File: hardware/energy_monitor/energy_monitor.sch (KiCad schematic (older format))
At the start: 138 parts, among them J1 Screw_Terminal_01x03, J2 Audio-Jack-3, J3 Audio-Jack-3, J4 Audio-Jack-3, J5 Audio-Jack-3, J6 Audio-Jack-3, J7 Audio-Jack-3, J8 USB_OTG, Q1 MMBT2222, Q2 MMBT2222, U1 RAC04, U2 TPS730, U3 TPS723, U4 ADS131E08, U5 AP2112, U6 ESP-WROOM-32D, U7 CP2104

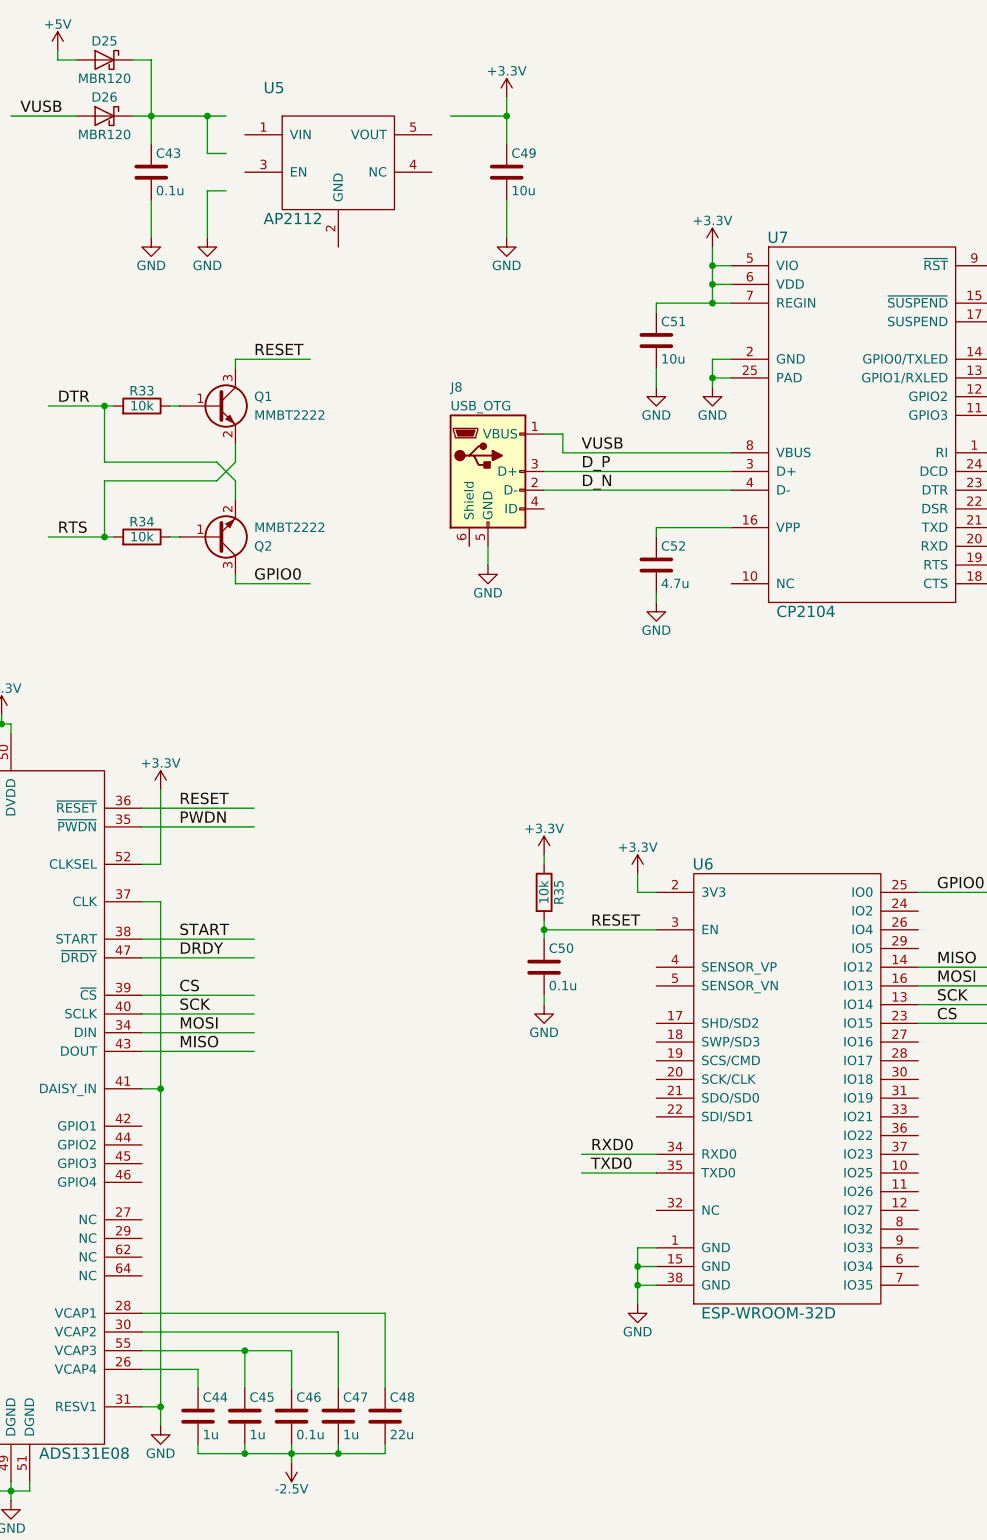
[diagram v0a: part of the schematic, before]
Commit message: Working on BOM and assigning footprints
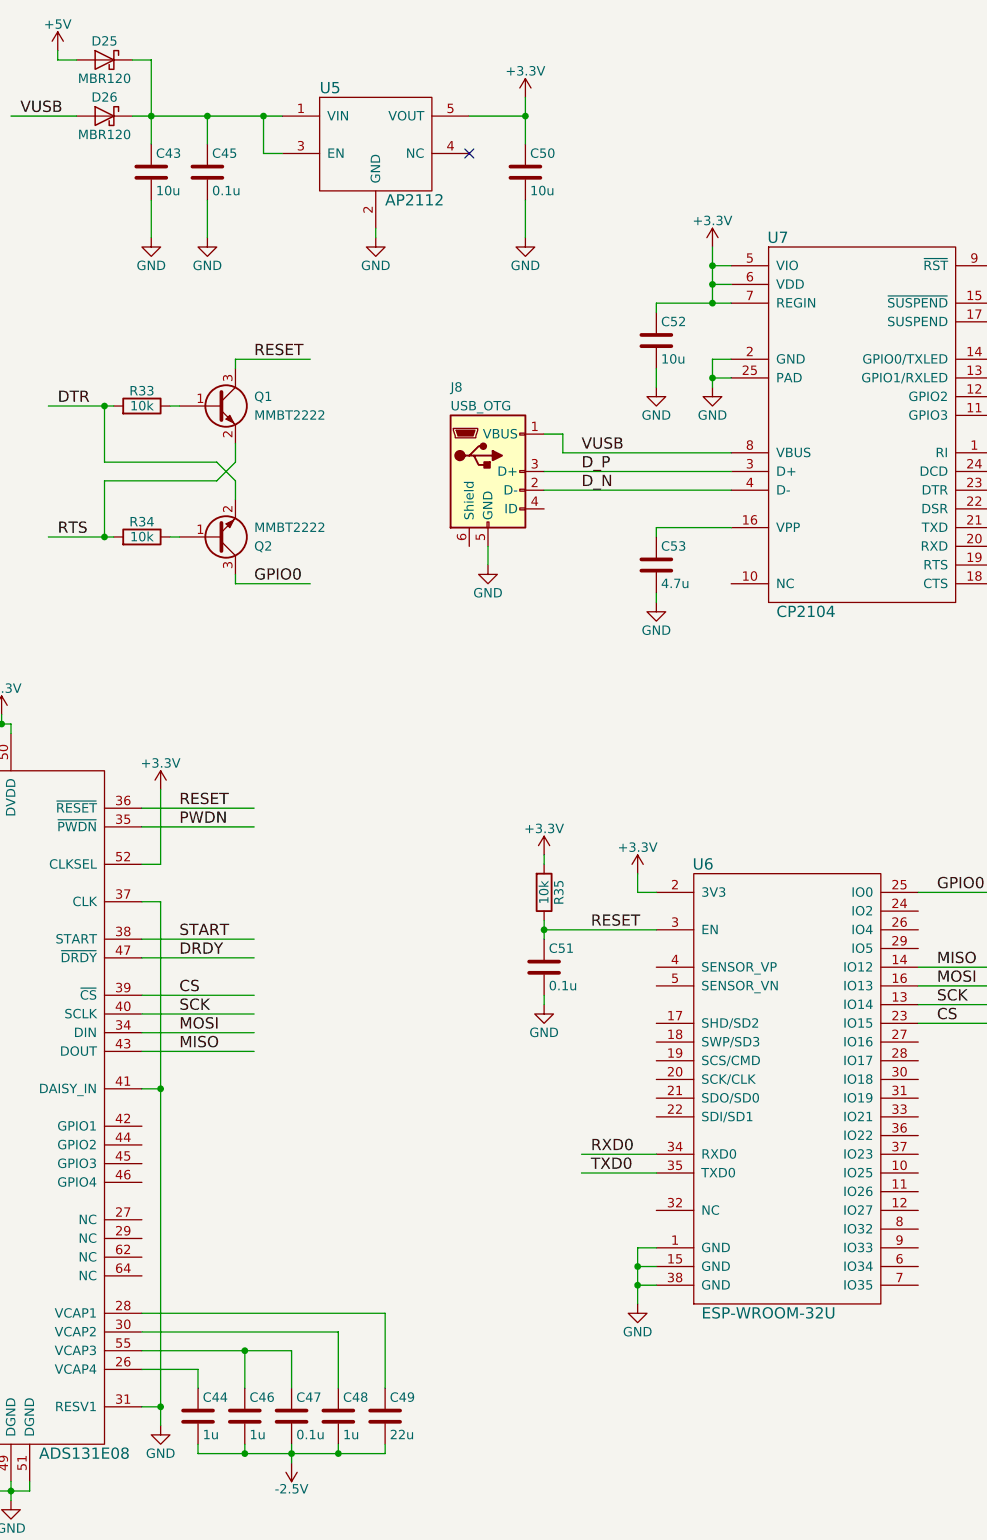
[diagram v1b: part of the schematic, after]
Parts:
- removed C49: 10u, symbol C
- added C48: 1u, Capacitors_SMD:C_0805, symbol C
- added C51: 0.1u, Capacitors_SMD:C_0603, symbol C
- C13, C14, C17, C32, C34, C37, C40, C42: footprint (none) -> Capacitors_SMD:C_0603; Part (none) -> 490-9691-1-ND; Source (none) -> DigiKey
- C15, C16: footprint (none) -> Capacitors_SMD:CP_Elec_6.3x5.8; Part (none) -> PCE3889CT-ND; Source (none) -> DigiKey
- C30, C36: footprint (none) -> Capacitors_SMD:C_0603; Part (none) -> 490-1520-1-ND; Source (none) -> DigiKey
- C31, C38: footprint (none) -> Capacitors_SMD:C_0805; Part (none) -> 490-11596-1-ND; Source (none) -> DigiKey
- C33: footprint (none) -> Capacitors_SMD:C_0805; Part (none) -> 490-5523-1-ND; Source (none) -> DigiKey
- C35, C39, C41, C44: footprint (none) -> Capacitors_SMD:C_0805; Part (none) -> 490-1691-1-ND; Source (none) -> DigiKey
- C43, C50: value 0.1u -> 10u; footprint (none) -> Capacitors_SMD:C_0805; Part (none) -> 490-5523-1-ND; Source (none) -> DigiKey
- C45, C47: value 1u -> 0.1u; footprint (none) -> Capacitors_SMD:C_0603; Part (none) -> 490-9691-1-ND; Source (none) -> DigiKey
- C46: value 0.1u -> 1u; footprint (none) -> Capacitors_SMD:C_0805; Part (none) -> 490-1691-1-ND; Source (none) -> DigiKey
- C49: renamed from C48; footprint (none) -> Capacitors_SMD:C_1206; Part (none) -> 490-8342-1-ND; Source (none) -> DigiKey
- C52: renamed from C51; footprint (none) -> Capacitors_SMD:C_0805; Part (none) -> 490-5523-1-ND; Source (none) -> DigiKey
- C53: renamed from C52; footprint (none) -> Capacitors_SMD:C_0805; Part (none) -> 490-5422-1-ND; Source (none) -> DigiKey
- D23, D27: Part (none) -> 160-1447-1-ND
- D24, D28: Part (none) -> 160-1435-1-ND
- D25, D26: footprint (none) -> footprint:SOD-123FL; Part (none) -> MBR120VLSFT3GOSCT-ND; Source (none) -> DigiKey
- F1, F2: footprint (none) -> Fuse_Holders_and_Fuses:Fuseholder5x20_horiz_open_inline_Type-I; Part (none) -> 486-2019-ND; Source (none) -> DigiKey
- J8: Part (none) -> H2959CT-ND; Source (none) -> DigiKey
- Q1, Q2: footprint (none) -> TO_SOT_Packages_SMD:SOT-23; Part (none) -> MMBT2222ALT3GOSCT-ND; Source (none) -> DigiKey
- R31, R32, R36, R37: Part (none) -> 311-1.00KHRCT-ND
- R33, R34, R35: footprint (none) -> Resistors_SMD:R_0603; Part (none) -> 311-10.0KHRCT-ND; Source (none) -> DigiKey
- RV1, RV2: footprint (none) -> Varistors:RV_Disc_D15.5_W6.8_P7.5
- U2, U3: footprint (none) -> TO_SOT_Packages_SMD:SOT-23-5
- U4: footprint (none) -> Housings_QFP:TQFP-64_10x10mm_Pitch0.5mm; Part (none) -> 296-43796-5-ND; Source (none) -> DigiKey
- U5: footprint (none) -> TO_SOT_Packages_SMD:SOT-23-5; Part (none) -> AP2112K-3.3TRG1DICT-ND; Source (none) -> DigiKey
- U6: value ESP-WROOM-32D -> ESP-WROOM-32U; footprint (none) -> footprint:ESP32-WROOM-32U; Source (none) -> DigiKey
- U7: footprint (none) -> Housings_DFN_QFN:QFN-24-1EP_4x4mm_Pitch0.5mm; Part (none) -> 336-2008-5-ND; Source (none) -> DigiKey
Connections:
- wire segments 430 -> 431
- no-connect marks 0 -> 1
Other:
- moved on the sheet: U5

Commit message: Working on footprints
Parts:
- removed J2, J3, J4, J5, J6, J7: Audio-Jack-3, symbol Audio-Jack-3
- added J2, J3, J4, J5, J6, J7: SJ1-3533NG, footprint:SJ1-3533NG, symbol SJ1-3533NG
- J1: Part 277-1118-ND -> 277-6062-ND

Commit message: Working on footprints
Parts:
- J1: footprint (none) -> footprint:1888690
- J8: footprint (none) -> footprint:UX60-MB-5ST
- U1: footprint (none) -> footprint:RAC04
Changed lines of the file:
@@
 F 0 "J1" H 900 1700 50  0000 C CNN
 F 1 "Screw_Terminal_01x03" H 900 1300 50  0001 C CNN
-F 2 "" H 900 1500 50  0001 C CNN
+F 2 "footprint:1888690" H 900 1500 50  0001 C CNN
 F 3 "" H 900 1500 50  0001 C CNN
 F 4 "DigiKey" H 900 1500 60  0001 C CNN "Source"
@@
 F 0 "U1" H 3000 2050 60  0000 L CNN
 F 1 "RAC04" H 3000 950 60  0000 L CNN
-F 2 "" H 3300 1500 60  0001 C CNN
+F 2 "footprint:RAC04" H 3300 1500 60  0001 C CNN
 F 3 "" H 3300 1500 60  0001 C CNN
 F 4 "DigiKey" H 3300 1500 60  0001 C CNN "Source"
@@
 F 0 "J8" H 12350 3550 50  0000 L CNN
 F 1 "USB_OTG" H 12350 3450 50  0000 L CNN
-F 2 "" H 12700 3050 50  0001 C CNN
+F 2 "footprint:UX60-MB-5ST" H 12700 3050 50  0001 C CNN
 F 3 "" H 12700 3050 50  0001 C CNN
 F 4 "DigiKey" H 12550 3100 60  0001 C CNN "Source"

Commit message: Working on layout
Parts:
- F1, F2: footprint Fuse_Holders_and_Fuses:Fuseholder5x20_horiz_open_inline_Type-I -> footprint:Fuse_Littelfuse-443; Part 486-2019-ND -> F2906CT-ND
- RV1, RV2: footprint Varistors:RV_Disc_D15.5_W6.8_P7.5 -> Varistors:RV_Disc_D12_W5_P7.5; Part 495-6609-ND -> P7207-ND
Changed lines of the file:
@@
 F 0 "F1" V 1630 1100 50  0000 C CNN
 F 1 "1A/300V" V 1475 1100 50  0000 C CNN
-F 2 "Fuse_Holders_and_Fuses:Fuseholder5x20_horiz_open_inline_Type-I" V 1480 1100 50  0001 C CNN
+F 2 "footprint:Fuse_Littelfuse-443" V 1480 1100 50  0001 C CNN
 F 3 "" H 1550 1100 50  0001 C CNN
 F 4 "DigiKey" H 1550 1100 60  0001 C CNN "Source"
-F 5 "486-2019-ND" H 1550 1100 60  0001 C CNN "Part"
+F 5 "F2906CT-ND" H 1550 1100 60  0001 C CNN "Part"
 	1    1550 1100
 	0    1    -1   0
@@
 F 0 "F2" V 1630 1900 50  0000 C CNN
 F 1 "1A/300V" V 1475 1900 50  0000 C CNN
-F 2 "Fuse_Holders_and_Fuses:Fuseholder5x20_horiz_open_inline_Type-I" V 1480 1900 50  0001 C CNN
+F 2 "footprint:Fuse_Littelfuse-443" V 1480 1900 50  0001 C CNN
 F 3 "" H 1550 1900 50  0001 C CNN
 F 4 "DigiKey" H 1550 1900 60  0001 C CNN "Source"
-F 5 "486-2019-ND" H 1550 1900 60  0001 C CNN "Part"
+F 5 "F2906CT-ND" H 1550 1900 60  0001 C CNN "Part"
 	1    1550 1900
 	0    1    -1   0
@@
 F 0 "RV1" H 2000 1350 50  0000 L CNN
 F 1 "MOV" H 2000 1250 50  0000 L CNN
-F 2 "Varistors:RV_Disc_D15.5_W6.8_P7.5" V 1830 1300 50  0001 C CNN
+F 2 "Varistors:RV_Disc_D12_W5_P7.5" V 1830 1300 50  0001 C CNN
 F 3 "" H 1900 1300 50  0001 C CNN
 F 4 "DigiKey" H 1900 1300 60  0001 C CNN "Source"
-F 5 "495-6609-ND" H 1900 1300 60  0001 C CNN "Part"
+F 5 "P7207-ND" H 1900 1300 60  0001 C CNN "Part"
 	1    1900 1300
 	1    0    0    -1
@@
 F 0 "RV2" H 2000 1750 50  0000 L CNN
 F 1 "MOV" H 2000 1650 50  0000 L CNN
-F 2 "Varistors:RV_Disc_D15.5_W6.8_P7.5" V 1830 1700 50  0001 C CNN
+F 2 "Varistors:RV_Disc_D12_W5_P7.5" V 1830 1700 50  0001 C CNN
 F 3 "" H 1900 1700 50  0001 C CNN
 F 4 "DigiKey" H 1900 1700 60  0001 C CNN "Source"
-F 5 "495-6609-ND" H 1900 1700 60  0001 C CNN "Part"
+F 5 "P7207-ND" H 1900 1700 60  0001 C CNN "Part"
 	1    1900 1700
 	1    0    0    -1

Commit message: Working on layout
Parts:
- C31, C38: value 2.2u -> 10u; Part 490-11596-1-ND -> 490-5523-1-ND
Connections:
- net labels added: GNDA, GNDD
- net labels removed: GND
- wire segments 431 -> 433

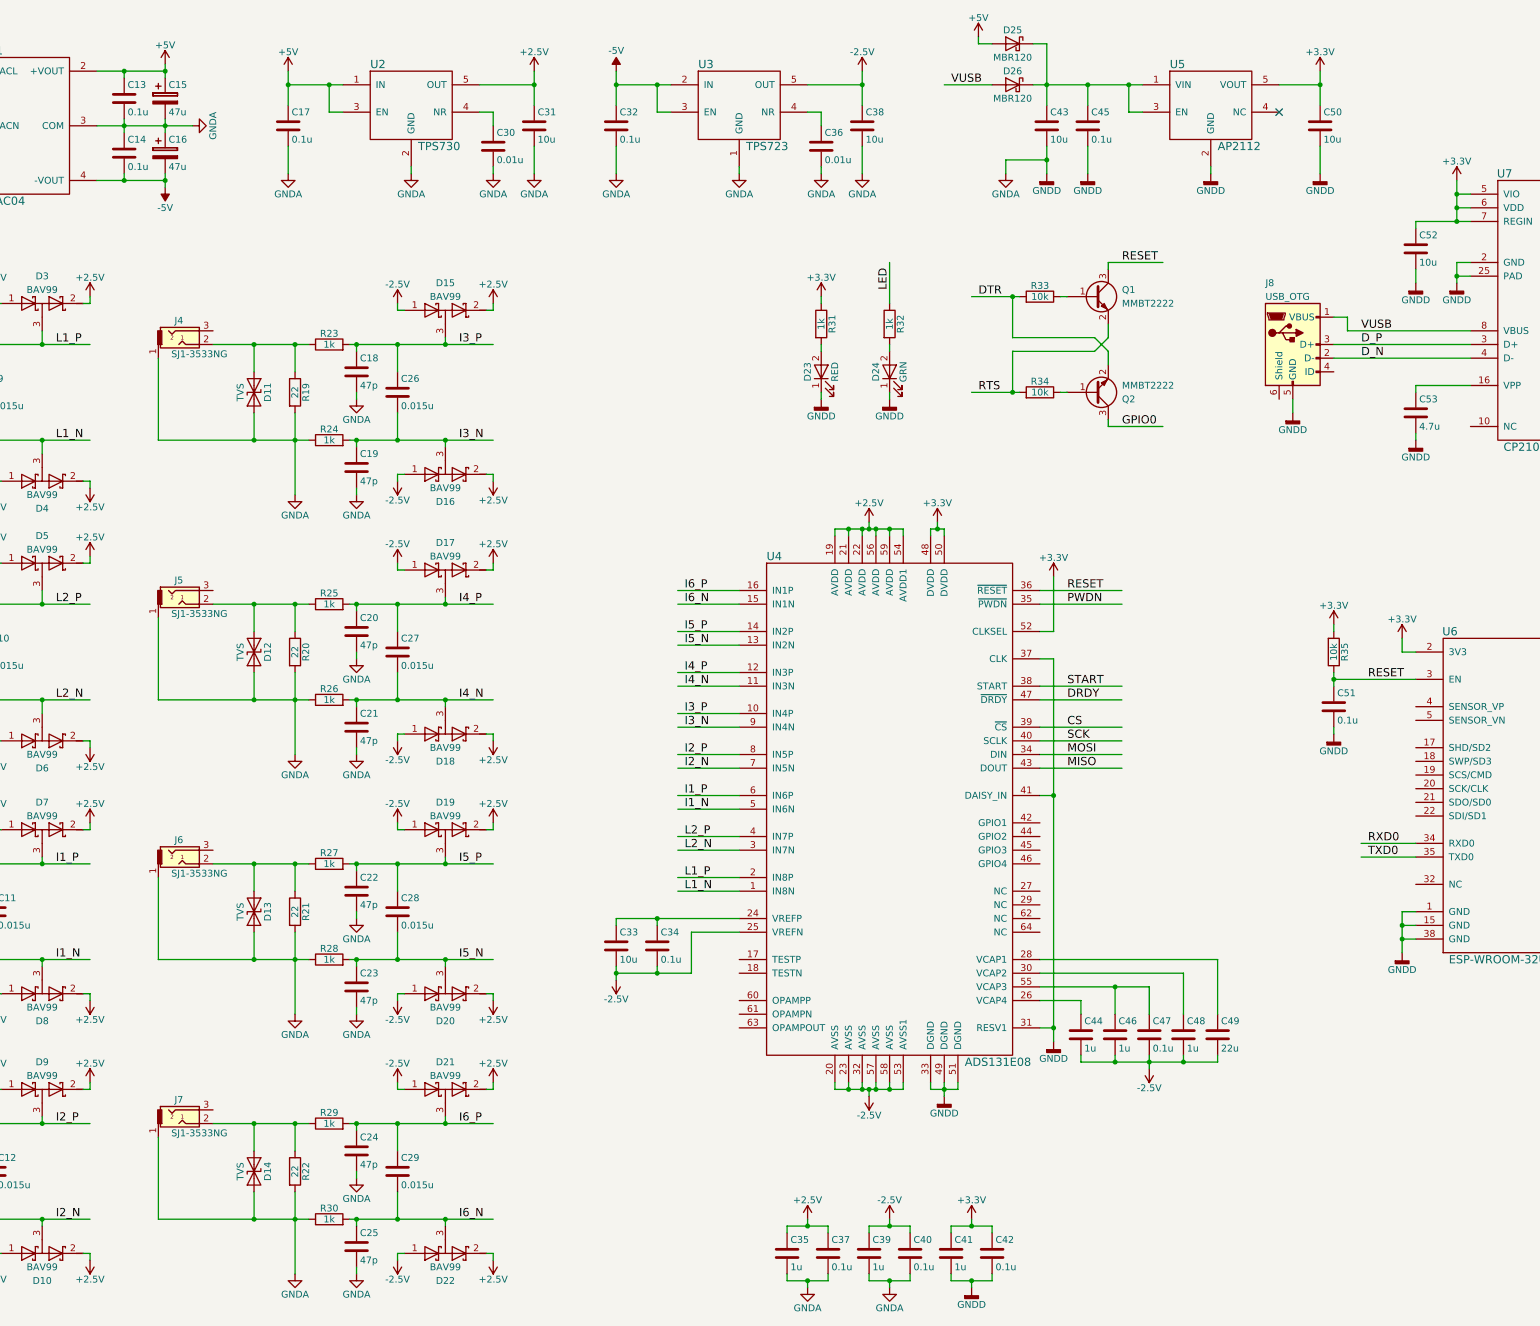
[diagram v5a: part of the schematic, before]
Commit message: Working on layout.  Removed 0.1u caps on 5V output
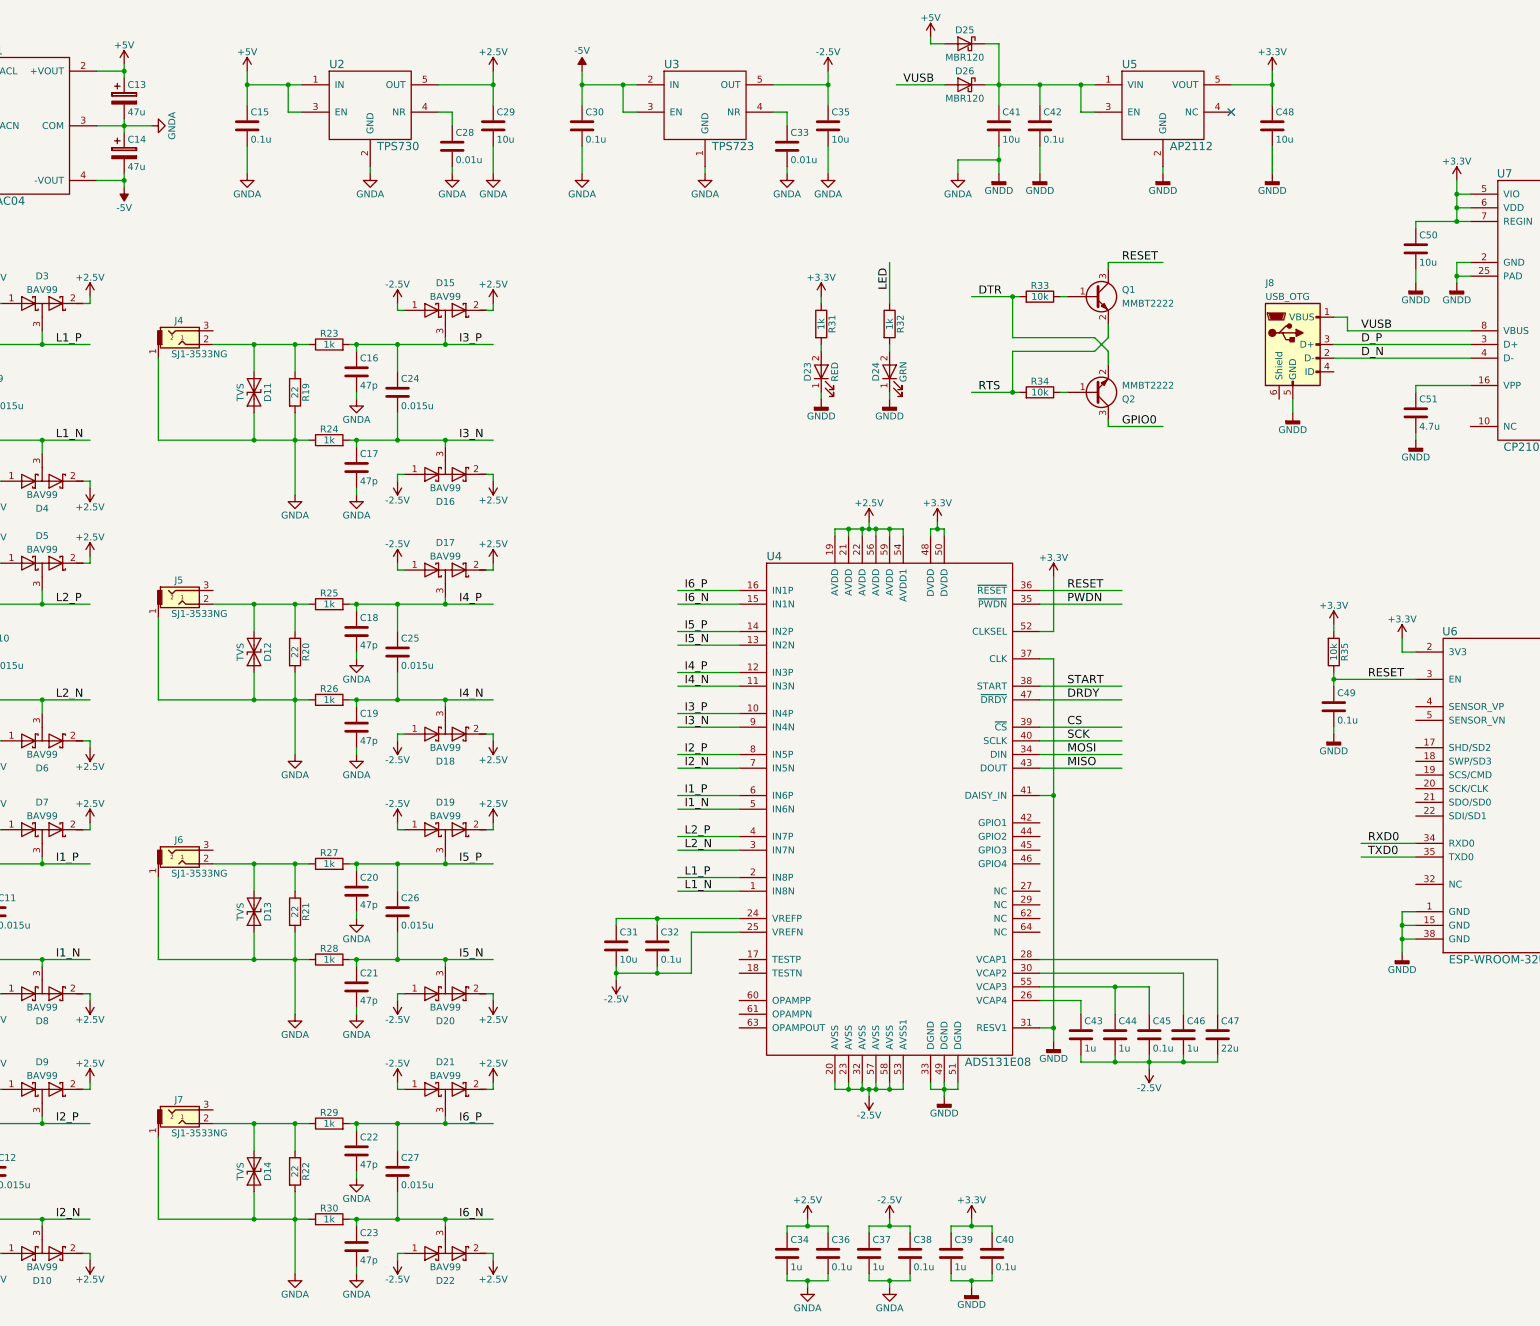
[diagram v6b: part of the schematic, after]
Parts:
- removed C13, C14: 0.1u, Capacitors_SMD:C_0603, symbol C
- renumbered C15 to C13, C16 to C14, C17 to C15, C18 to C16, C19 to C17, C20 to C18, C21 to C19, C22 to C20, C23 to C21, C24 to C22, C25 to C23, C26 to C24, C27 to C25, C28 to C26, C29 to C27, C30 to C28, C31 to C29, C32 to C30, C33 to C31, C34 to C32, C36 to C33, C35 to C34, C38 to C35, C37 to C36, C39 to C37, C40 to C38, C41 to C39, C42 to C40, C43 to C41, C45 to C42, C44 to C43, C46 to C44, C47 to C45, C48 to C46, C49 to C47, C50 to C48, C51 to C49, C52 to C50, C53 to C51
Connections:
- wire segments 433 -> 430
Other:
- moved on the sheet: C13, C14, C15, C28, C29, C30, C33, C35, C41, C42, C48, D25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

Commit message: Switched 3.5mm jacks to terminal blocks
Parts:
- removed J2, J3, J4, J5, J6, J7: SJ1-3533NG, footprint:SJ1-3533NG, symbol SJ1-3533NG
- added J2, J3, J4: Screw_Terminal_01x04, footprint:TerminalBlock_04x5.08mm, symbol Screw_Terminal_01x04
- J1: footprint footprint:1888690 -> footprint:TerminalBlock_03x5.08mm; Part 277-6062-ND -> 277-1264-ND
- renumbered C48 to C47, C47 to C48, J8 to J5, U7 to U6, U6 to U7
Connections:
- wire segments 430 -> 448
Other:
- moved on the sheet: C16, C17, C18, C19, C20, C21, C22, C23, C24, C25, C26, C27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
